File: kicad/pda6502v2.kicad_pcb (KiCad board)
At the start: 4 copper layers, 100 x 100 mm, 89 parts, among them J1 GPIO1, J2 GPIO2, J3 UART, J4 Screw_Terminal_01x02, J5 Conn_02x04_Odd_Even, J6 ICSP, J7 SPI, J8 FPGA_EXT, J9 SID, SW1 SW_Push, U1 W65C02SxP, U10 LT3030, U11 SC28L92A1B, U2 W65C22SxP, U3 W65C22SxP, U4 DS1818, U5 AS6C4008-55PCN, U6 ARMSID, U7 AT25M01, U8 ICE40HX4K-TQ144, U9 TLV1117-33, X1 8 MHz, X2 3.6864 MHz

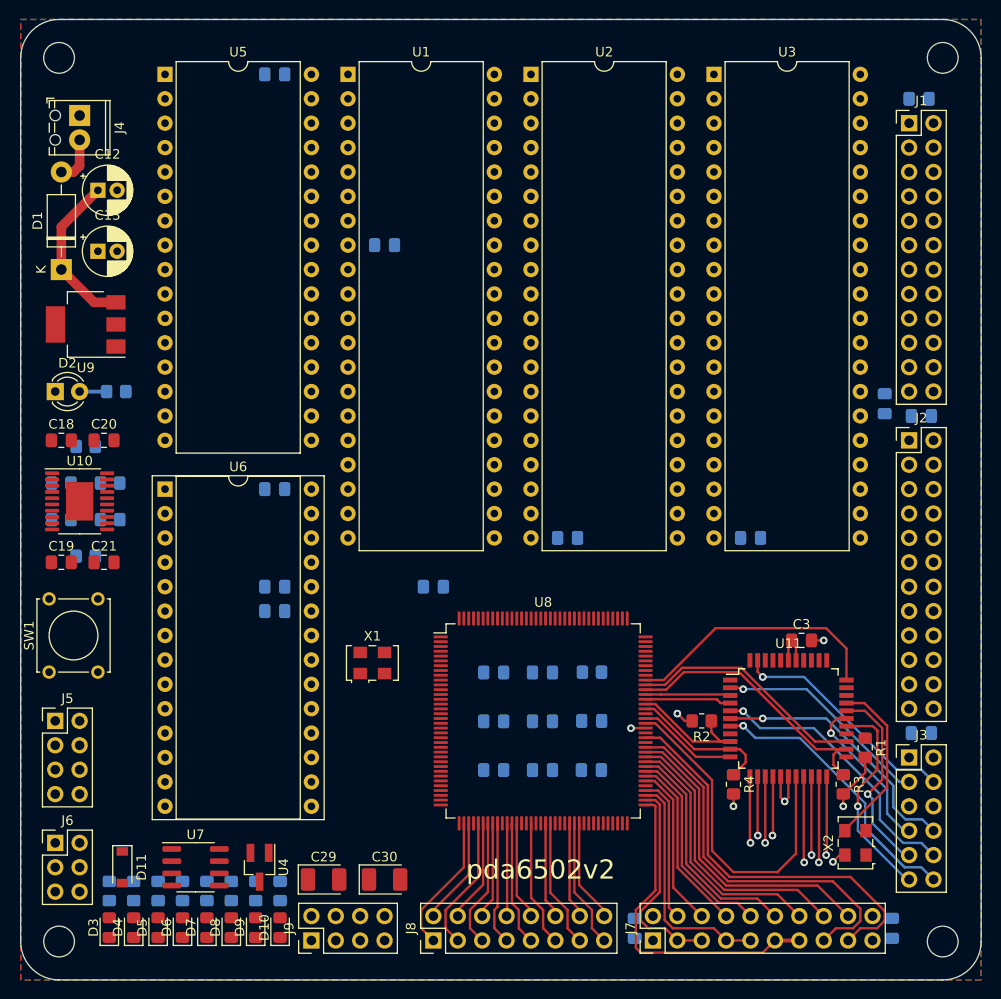
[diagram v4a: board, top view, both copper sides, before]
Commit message: LDO placement/routing, XO HandSolder footprint, etc.
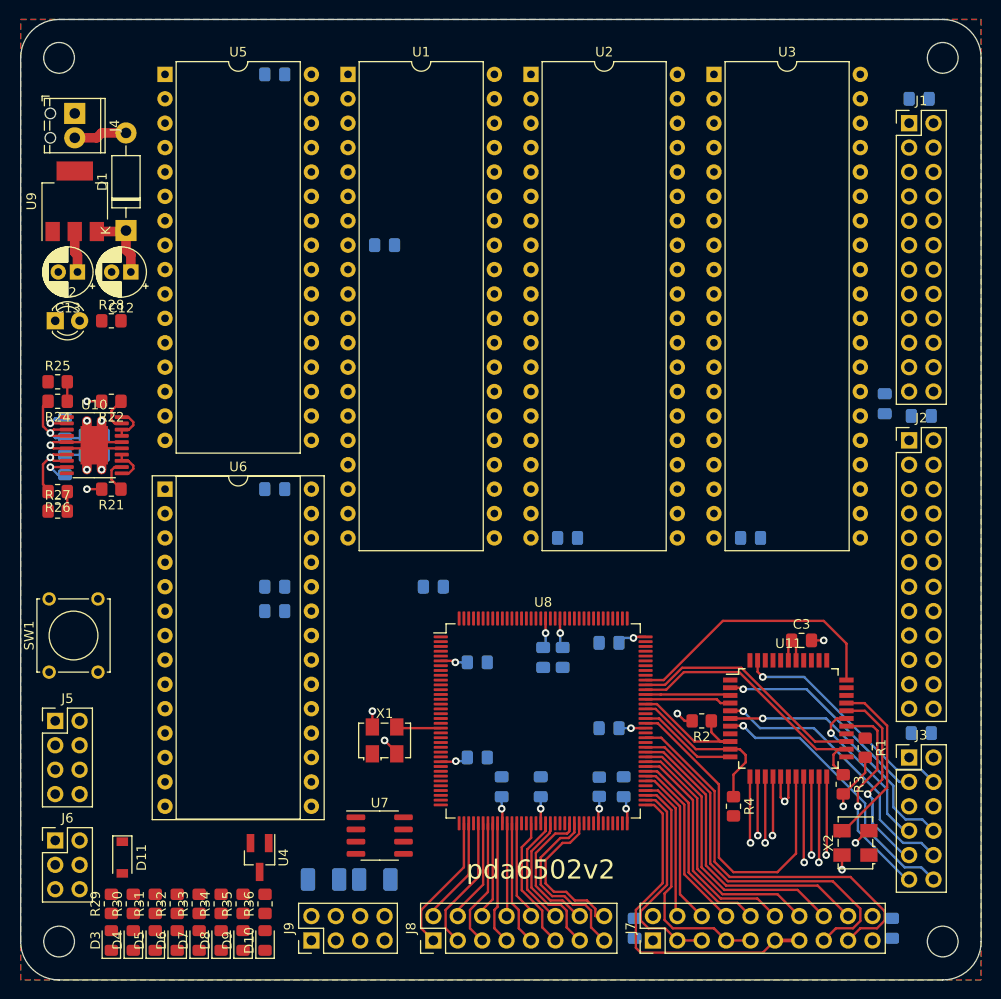
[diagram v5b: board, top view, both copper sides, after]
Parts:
- added C32: 0.1μF, Capacitor_SMD:C_0805_2012Metric_Pad1.18x1.45mm_HandSolder, B.Cu at (152.1, 119.9)
- C18, C19, C20, C21, C29, C30: moved to B.Cu
- R21, R22, R24, R25, R26, R27, R28, R29, R30, R31, R32, R33, R34, R35, R36: moved to F.Cu
- X1, X2: footprint Oscillator:Oscillator_SMD_EuroQuartz_XO53-4Pin_5.0x3.2mm -> pda6502v2:Oscillator_SMD_5.0x3.2mm_HandSolder
- moved U7 19.5 mm to (135.4, 125.0)
- moved C22 13.4 mm to (145.5, 106.9)
- moved U9 12.9 mm to (103.6, 58.9), turned to 90 degrees
- moved C14 12.8 mm to (159.3, 113.8), turned to 180 degrees
- moved R23 12.0 mm to (158.2, 119.9), turned to 90 degrees
- moved C11 11.9 mm to (154.4, 106.4), turned to 270 degrees
- moved C21 11.2 mm to (105.7, 85.3)
- moved C19 10.2 mm to (102.6, 86.4), turned to 270 degrees
- moved C12 9.17 mm to (109.5, 66.3), turned to 180 degrees
- moved C16 9.01 mm to (145.5, 116.8)
- moved R24 8.52 mm to (101.9, 79.8), turned to 180 degrees
- moved R22 8.51 mm to (107.4, 79.8), turned to 180 degrees
- moved X1 8.16 mm to (135.9, 115.1)
- moved D1 7.86 mm to (109.0, 62.0)
- moved C24 7.59 mm to (159.3, 104.9), turned to 180 degrees
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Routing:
- net GND: track 6.77 -> 40.8 mm, vias 2 -> 9
- net +3V3: track 16.8 -> 45.9 mm, vias 5 -> 11
- net +1V2: track 0.00 -> 20.3 mm, vias 0 -> 4
- net +2V5: track 0.00 -> 14.5 mm, vias 0 -> 2
- net +5V: track 16.9 -> 7.60 mm
- net /EXT_15: track 10.7 -> 16.1 mm
- net /EXT_14: track 13.5 -> 18.4 mm
- net /CLOCKSRC: track 0.00 -> 4.65 mm
- net /EXT_13: track 10.1 -> 14.6 mm
- net Net-(R21-Pad1): track 0.00 -> 3.57 mm
- net Net-(R22-Pad1): track 0.00 -> 3.57 mm
- net Net-(C19-Pad2): track 0.00 -> 3.56 mm, vias 0 -> 1
- net Net-(C18-Pad2): track 0.00 -> 3.46 mm, vias 0 -> 1
- net /~RESET: track 0.00 -> 2.84 mm, vias 0 -> 1
- net Net-(D2-Pad2): track 2.81 -> 0.00 mm
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
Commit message: Routing; power, ground vias, UART/osc, reset button/header, etc.
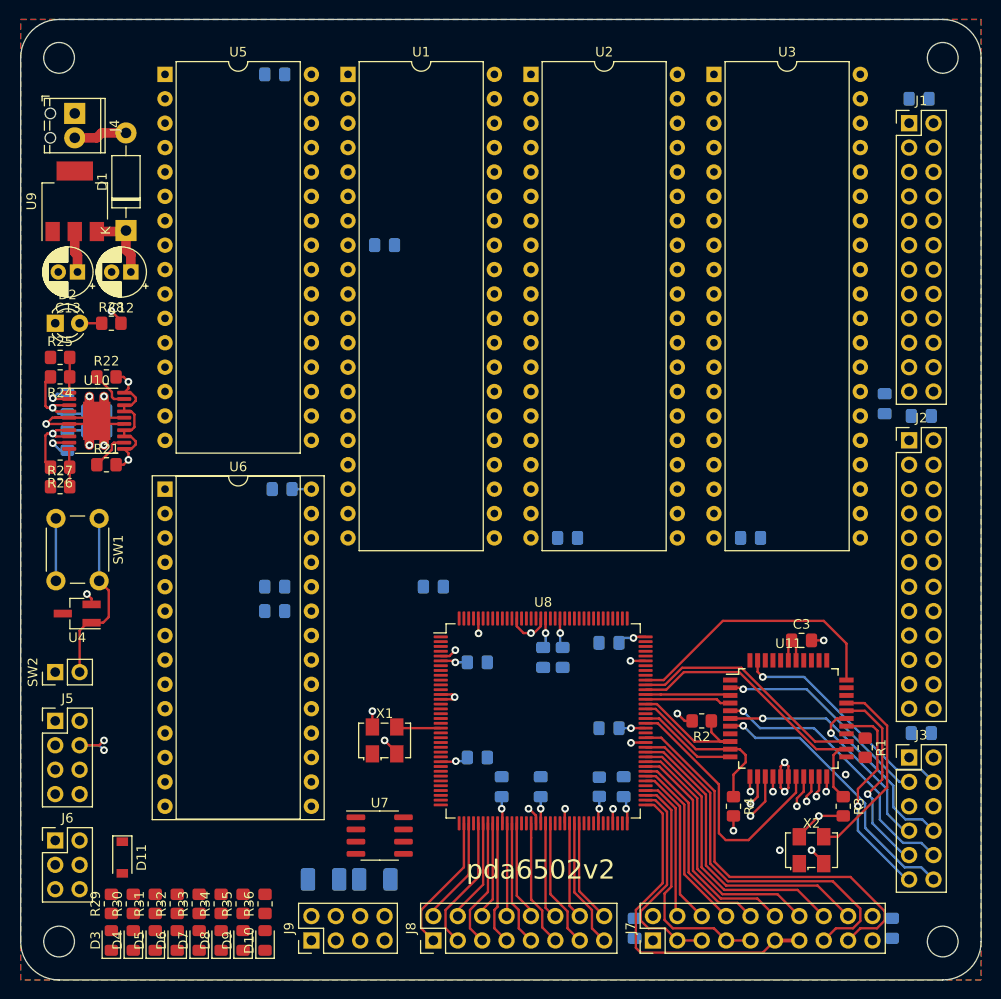
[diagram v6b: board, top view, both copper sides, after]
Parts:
- added SW2: SW_Push, Connector_PinHeader_2.54mm:PinHeader_1x02_P2.54mm_Vertical, F.Cu at (101.6, 108.0)
- SW1: footprint Button_Switch_THT:SW_Tactile_Straight_KSA0Axx1LFTR -> Button_Switch_THT:SW_PUSH_6mm_H5mm
- moved U4 31.7 mm to (103.9, 101.9), turned to 180 degrees
- moved SW1 16.8 mm to (106.2, 91.9), turned to 270 degrees
- moved X2 4.64 mm to (180.3, 126.5), turned to 0 degrees
- moved R21 2.59 mm to (106.9, 86.4), turned to 0 degrees
- moved R22 2.59 mm to (106.9, 77.2), turned to 0 degrees
- moved C19 2.55 mm to (102.9, 83.8)
- moved R24 2.55 mm to (102.1, 77.2)
- moved R25 2.55 mm to (102.1, 75.2)
- moved R27 2.55 mm to (102.1, 88.6)
- moved U10 2.55 mm to (105.9, 81.8)
- moved C18 2.55 mm to (102.9, 80.0)
- moved C20 2.55 mm to (105.9, 80.8)
- moved C21 2.55 mm to (105.9, 82.8)
- moved R26 2.55 mm to (102.1, 86.6)
- moved R3 2.29 mm to (183.6, 121.9)
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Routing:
- net +2V5: track 14.5 -> 125.9 mm
- net +5V: track 7.60 -> 90.8 mm
- net +1V2: track 20.3 -> 97.1 mm
- net GND: track 40.8 -> 70.7 mm, vias 9 -> 21
- net /~RESET: track 2.84 -> 21.5 mm
- net +3V3: track 45.9 -> 61.5 mm, vias 11 -> 15
- net /UART_~IRQ: track 35.4 -> 27.4 mm
- net /D2: track 8.95 -> 2.19 mm
- net /D0: track 8.20 -> 1.60 mm
- net /D6: track 8.96 -> 3.39 mm
- net /D4: track 8.18 -> 2.79 mm
- net /EXT_15: track 16.1 -> 10.7 mm
- net /D1: track 6.93 -> 1.58 mm
- net /EXT_14: track 18.4 -> 13.5 mm
- net /D7: track 6.16 -> 1.57 mm
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
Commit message: BLINKEN and other minor tweaks
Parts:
- C29, C30: moved to F.Cu
- R29, R30, R31, R32, R33, R34, R35, R36: moved to B.Cu
- moved U7 24.8 mm to (111.0, 129.5)
- moved D11 7.42 mm to (107.7, 119.9), turned to 90 degrees
- moved X1 4.68 mm to (134.9, 110.5)
- moved R29 3.05 mm to (107.4, 135.1)
- moved R30 3.05 mm to (109.7, 135.1)
- moved R31 3.05 mm to (112.0, 135.1)
- moved R32 3.05 mm to (114.3, 135.1)
- moved R33 3.05 mm to (116.6, 135.1)
- moved R34 3.05 mm to (118.9, 135.1)
- moved R35 3.05 mm to (121.2, 135.1)
- moved R36 3.05 mm to (123.4, 135.1)
- moved D10 0.76 mm to (123.4, 135.1), turned to 270 degrees
- moved D3 0.76 mm to (107.4, 135.1), turned to 270 degrees
- moved D4 0.76 mm to (109.7, 135.1), turned to 270 degrees
- moved D5 0.76 mm to (112.0, 135.1), turned to 270 degrees
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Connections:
- net Net-(C10-Pad1) renamed /VCC_FLASH
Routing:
- net /CLOCKSRC: track 4.65 -> 7.79 mm
- net Net-(D9-Pad2): track 0.00 -> 2.55 mm, vias 0 -> 1
- net Net-(D8-Pad2): track 0.00 -> 2.55 mm, vias 0 -> 1
- net Net-(D7-Pad2): track 0.00 -> 2.55 mm, vias 0 -> 1
- net Net-(D6-Pad2): track 0.00 -> 2.55 mm, vias 0 -> 1
- net Net-(D5-Pad2): track 0.00 -> 2.55 mm, vias 0 -> 1
- net Net-(D4-Pad2): track 0.00 -> 2.55 mm, vias 0 -> 1
- net Net-(D3-Pad2): track 0.00 -> 2.55 mm, vias 0 -> 1
- net Net-(D10-Pad2): track 0.00 -> 2.55 mm, vias 0 -> 1
- net Net-(U11-Pad30): track 20.4 -> 20.9 mm

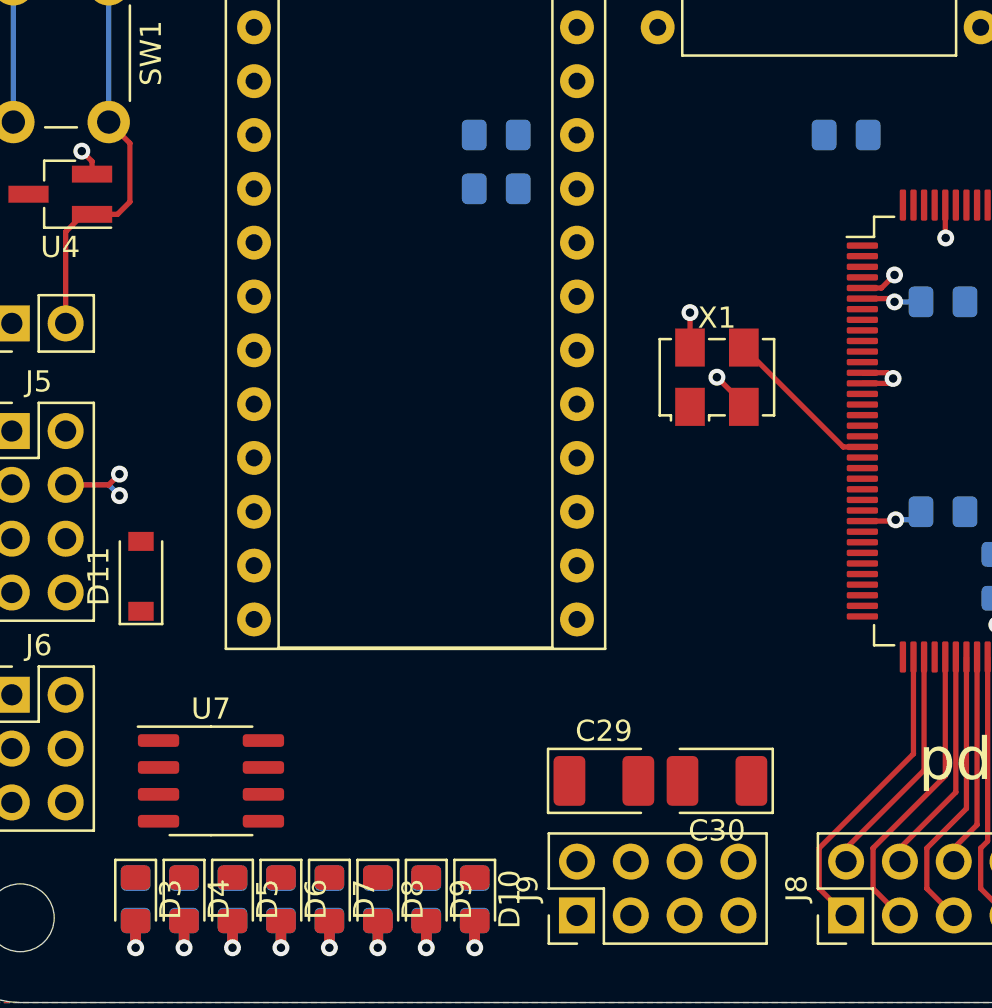
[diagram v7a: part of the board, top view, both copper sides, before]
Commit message: BLINKEN routed
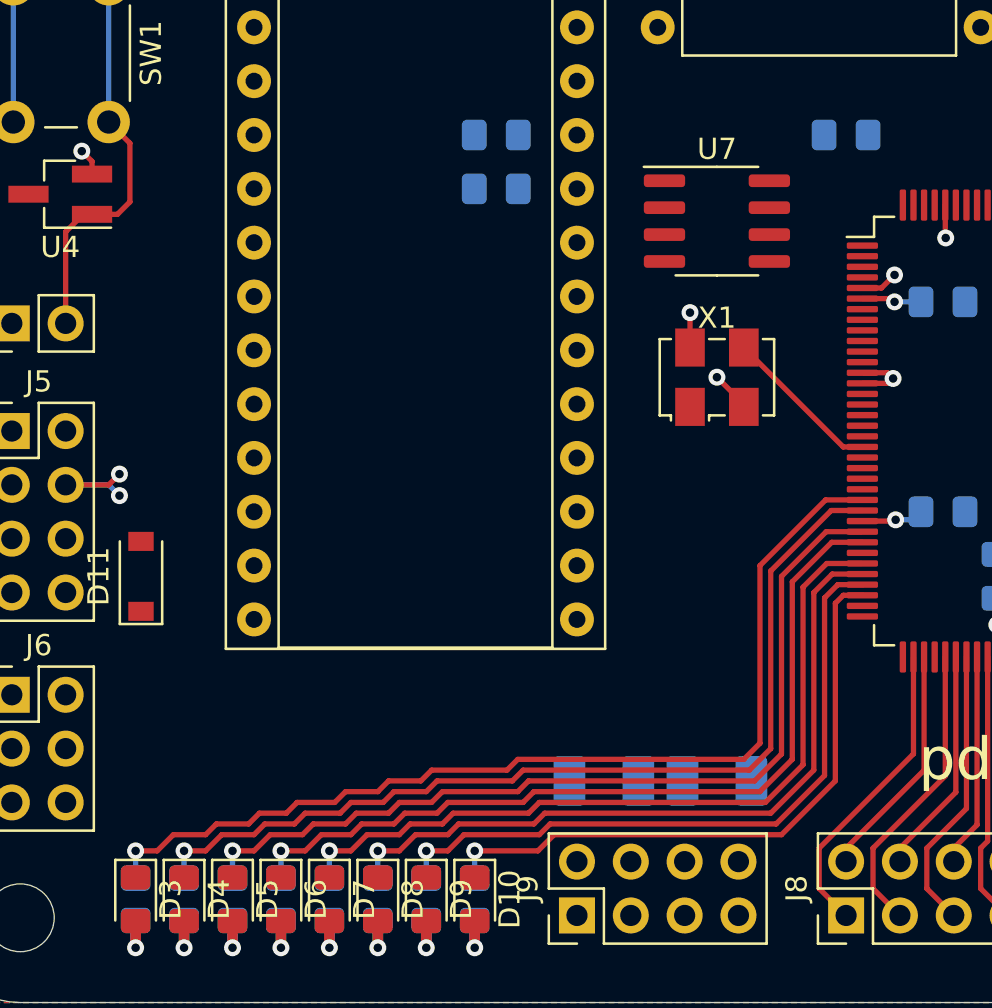
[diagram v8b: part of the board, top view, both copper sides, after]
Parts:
- C29, C30: moved to B.Cu
- moved U7 35.6 mm to (134.9, 103.1)
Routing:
- net /BLINKEN0: track 0.00 -> 47.4 mm, vias 0 -> 1
- net /BLINKEN1: track 0.00 -> 44.9 mm, vias 0 -> 1
- net /BLINKEN2: track 0.00 -> 42.2 mm, vias 0 -> 1
- net /BLINKEN3: track 0.00 -> 39.7 mm, vias 0 -> 1
- net /BLINKEN4: track 0.00 -> 37.0 mm, vias 0 -> 1
- net /BLINKEN5: track 0.00 -> 34.5 mm, vias 0 -> 1
- net /BLINKEN6: track 0.00 -> 32.0 mm, vias 0 -> 1
- net /BLINKEN7: track 0.00 -> 29.5 mm, vias 0 -> 1
